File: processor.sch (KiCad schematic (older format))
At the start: 47 parts, among them J4 USB_C_Receptacle_USB2.0, Q5 2N7002, Q6 BC817-40, Q7 BC817-40, U3 ESP32-WROOM-32D, U6 USBLC6-2SC6, U7 TPS560200, U8 CP2102N-A01-GQFN24

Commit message: Clean up rescued symbols and reneabled layer visibility
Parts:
- J4: symbol stack-light-rescue:USB_C_Receptacle_USB2.0-Connector -> Connector:USB_C_Receptacle_USB2.0
- U6: symbol stack-light-rescue:USBLC6-2SC6-Power_Protection -> Power_Protection:USBLC6-2SC6
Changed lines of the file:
@@
 	8800 2000 8800 2100
 $Comp
-L stack-light-rescue:USB_C_Receptacle_USB2.0-Connector J4
+L Connector:USB_C_Receptacle_USB2.0 J4
 U 1 1 5DB0CA37
 P 1650 6500
@@
 Wire Wire Line
 	2250 6400 2250 6500
-Connection ~ 2250 6500
 Wire Wire Line
 	2250 6700 2250 6600
-Connection ~ 2250 6600
 $Comp
 L power:GND #PWR0157
@@
 	2600 6100 2750 6100
 $Comp
-L stack-light-rescue:USBLC6-2SC6-Power_Protection U6
+L Power_Protection:USBLC6-2SC6 U6
 U 1 1 6039A5CC
 P 3150 7050
@@
 	2250 6600 3650 6600
 Wire Wire Line
-	3150 5900 3150 6550
-Wire Wire Line
 	3650 6950 3650 6600
 Wire Wire Line
-	2650 6950 2500 6950
-Wire Wire Line
 	2500 6950 2500 6500
 Wire Wire Line
-	2650 7150 2600 7150
-Wire Wire Line
 	2600 6500 4400 6500
 Wire Wire Line
 	2600 6500 2600 7150
-Wire Wire Line
-	3650 7150 3750 7150
 Wire Wire Line
 	3750 7150 3750 6600
@@
 	1    0    0    -1
 $EndComp
+Wire Wire Line
+	2500 6950 2750 6950
+Wire Wire Line
+	2600 7150 2750 7150
+Wire Wire Line
+	3150 7550 3150 7450
+Wire Wire Line
+	3550 7150 3750 7150
+Wire Wire Line
+	3650 6950 3550 6950
+Wire Wire Line
+	3150 5900 3150 6650
 $EndSCHEMATC

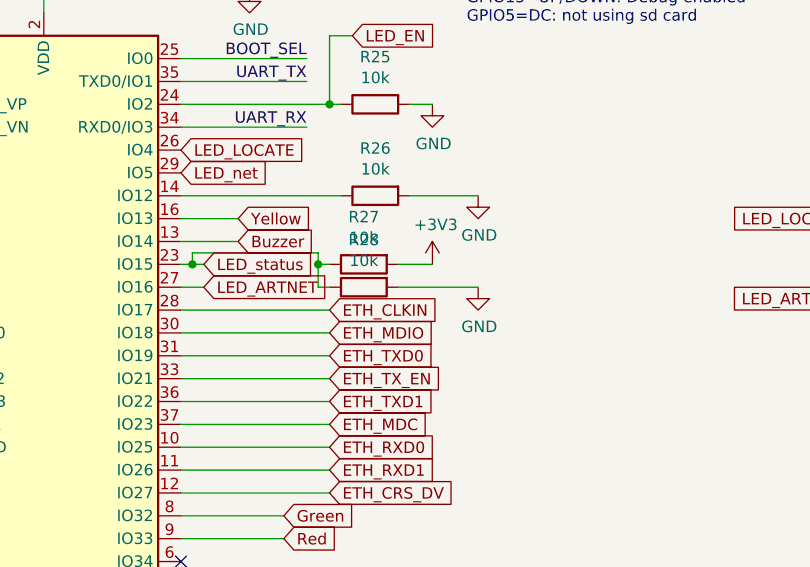
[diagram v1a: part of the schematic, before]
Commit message: Add minor fixes for r1.0 issues
Add load resistors for POE power supply
Add pulldown for buzzer output channel
Mark debug boot resistor as DNP
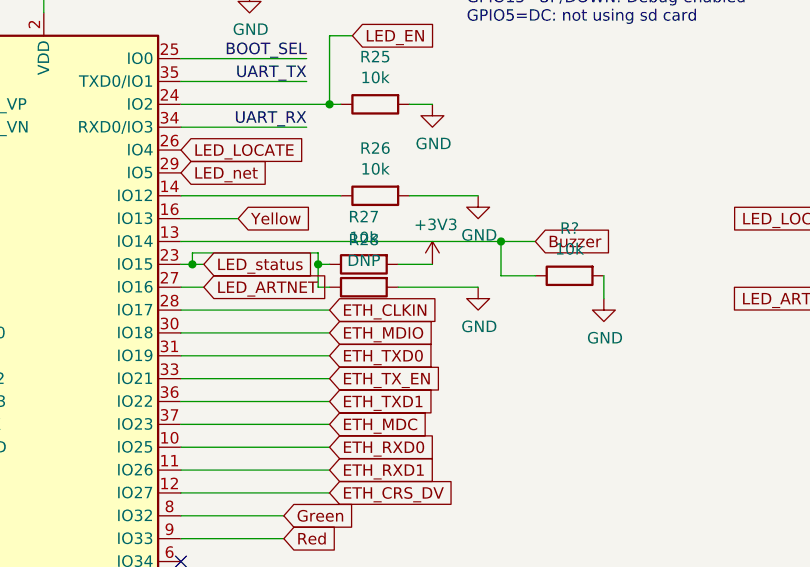
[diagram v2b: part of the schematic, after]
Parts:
- added R?: 10k, Resistor_SMD:R_0603_1608Metric, symbol Device:R
- R28: value 10k -> DNP
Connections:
- net Buzzer: now also R?.1
- net GND: now also R?.2
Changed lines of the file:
@@
 AR Path="/5DEE5ACA/602A9C12" Ref="R28"  Part="1"
 F 0 "R28" V 3693 2400 50  0000 C CNN
-F 1 "10k" V 3784 2400 50  0000 C CNN
+F 1 "DNP" V 3784 2400 50  0000 C CNN
 F 2 "Resistor_SMD:R_0603_1608Metric" V 3830 2400 50  0001 C CNN
 F 3 "~" H 3900 2400 50  0001 C CNN
@@
 Text GLabel 3550 3400 2    50   Input ~ 0
 Green
-Text GLabel 3350 2200 2    50   Input ~ 0
+Text GLabel 4650 2200 2    50   Input ~ 0
 Buzzer
 Text Label 3800 6500 0    50   ~ 0
@@
 	3750 6600 4850 6600
 Wire Wire Line
-	3350 2200 3100 2200
-Wire Wire Line
 	3350 2100 3100 2100
 $Comp
@@
 Wire Wire Line
 	3150 5900 3150 6650
+$Comp
+L Device:R R?
+U 1 1 60A94591
+P 4800 2350
+AR Path="/60A94591" Ref="R?"  Part="1"
+AR Path="/5DEE5ACA/60A94591" Ref="R?"  Part="1"
+F 0 "R?" V 4593 2350 50  0000 C CNN
+F 1 "10k" V 4684 2350 50  0000 C CNN
+F 2 "Resistor_SMD:R_0603_1608Metric" V 4730 2350 50  0001 C CNN
+F 3 "~" H 4800 2350 50  0001 C CNN
+	1    4800 2350
+	0    -1   1    0
+$EndComp
+$Comp
+L power:GND #PWR?
+U 1 1 60A94AE4
+P 4950 2450
+F 0 "#PWR?" H 4950 2200 50  0001 C CNN
+F 1 "GND" H 4955 2277 50  0000 C CNN
+F 2 "" H 4950 2450 50  0001 C CNN
+F 3 "" H 4950 2450 50  0001 C CNN
+	1    4950 2450
+	1    0    0    -1
+$EndComp
+Wire Wire Line
+	4950 2450 4950 2350
+Wire Wire Line
+	4650 2350 4500 2350
+Wire Wire Line
+	4500 2350 4500 2200
+Wire Wire Line
+	4500 2200 4650 2200
+Wire Wire Line
+	3100 2200 4500 2200
+Connection ~ 4500 2200
 $EndSCHEMATC

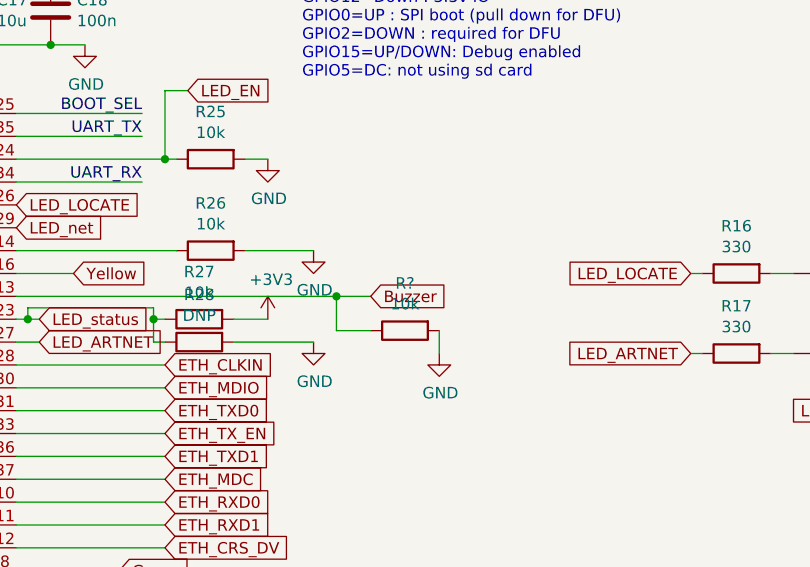
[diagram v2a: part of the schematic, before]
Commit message: Add schematic edits to PCB
Add load resistors for POE power supply
Add pulldown for buzzer output channel
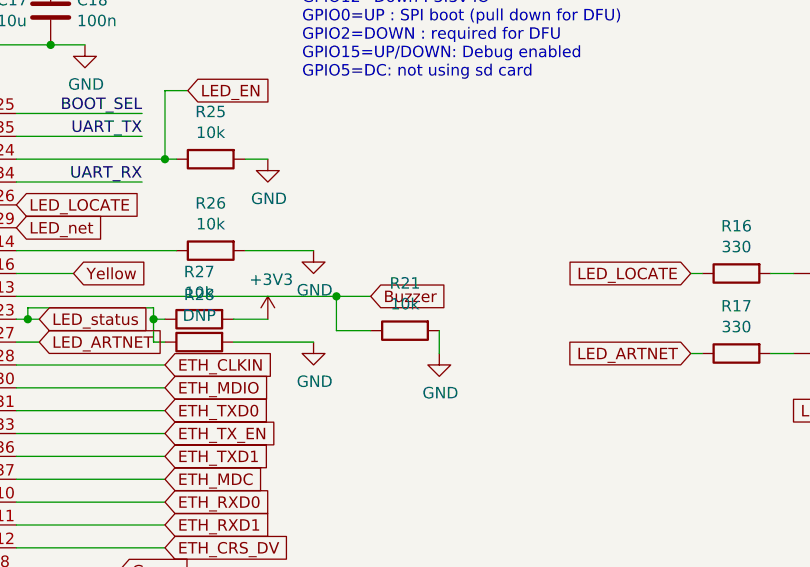
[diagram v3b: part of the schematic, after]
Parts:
- gave numbers to parts that had none: 1
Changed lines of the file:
@@
 P 4800 2350
 AR Path="/60A94591" Ref="R?"  Part="1"
-AR Path="/5DEE5ACA/60A94591" Ref="R?"  Part="1"
-F 0 "R?" V 4593 2350 50  0000 C CNN
+AR Path="/5DEE5ACA/60A94591" Ref="R21"  Part="1"
+F 0 "R21" V 4593 2350 50  0000 C CNN
 F 1 "10k" V 4684 2350 50  0000 C CNN
 F 2 "Resistor_SMD:R_0603_1608Metric" V 4730 2350 50  0001 C CNN
@@
 $EndComp
 $Comp
-L power:GND #PWR?
+L power:GND #PWR0158
 U 1 1 60A94AE4
 P 4950 2450
-F 0 "#PWR?" H 4950 2200 50  0001 C CNN
+F 0 "#PWR0158" H 4950 2200 50  0001 C CNN
 F 1 "GND" H 4955 2277 50  0000 C CNN
 F 2 "" H 4950 2450 50  0001 C CNN

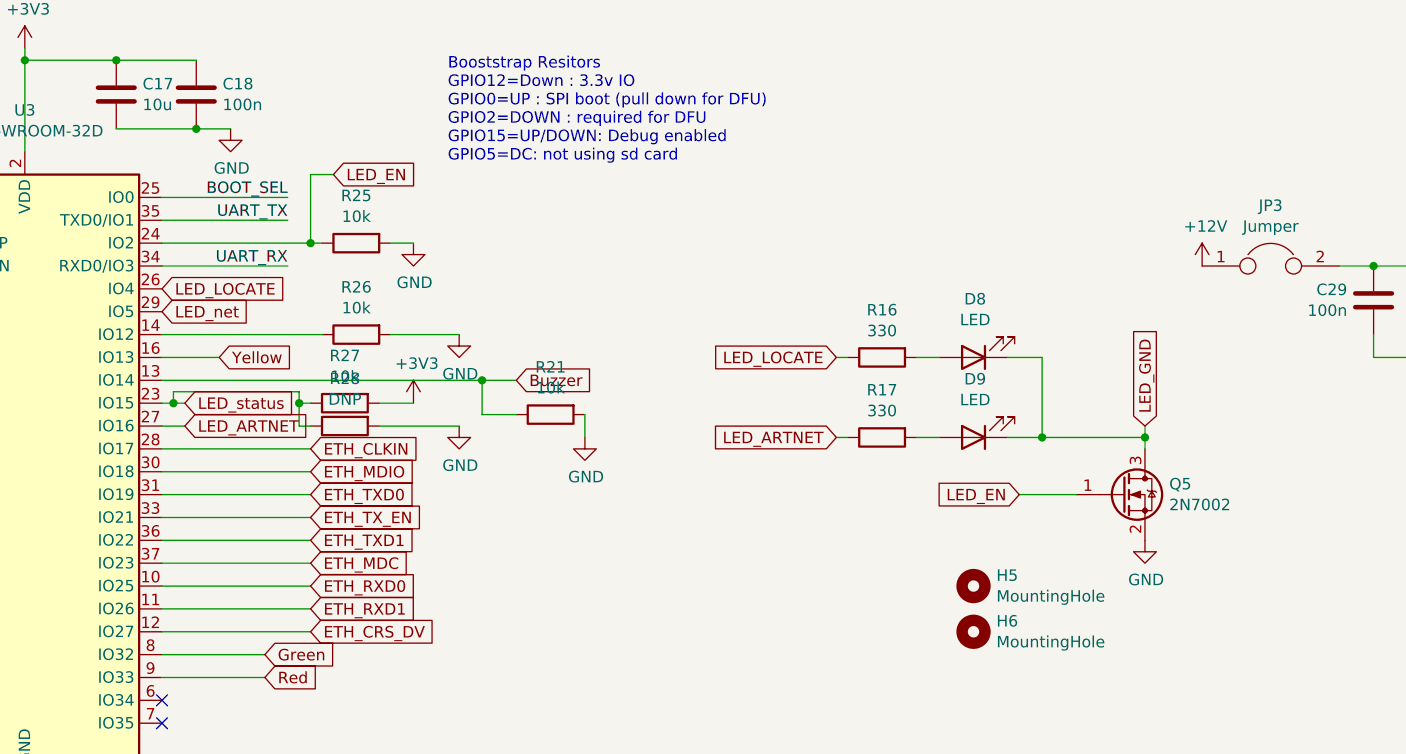
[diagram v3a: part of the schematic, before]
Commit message: Adjust front IO to work with a flush panel
also removed the LED enable transistor
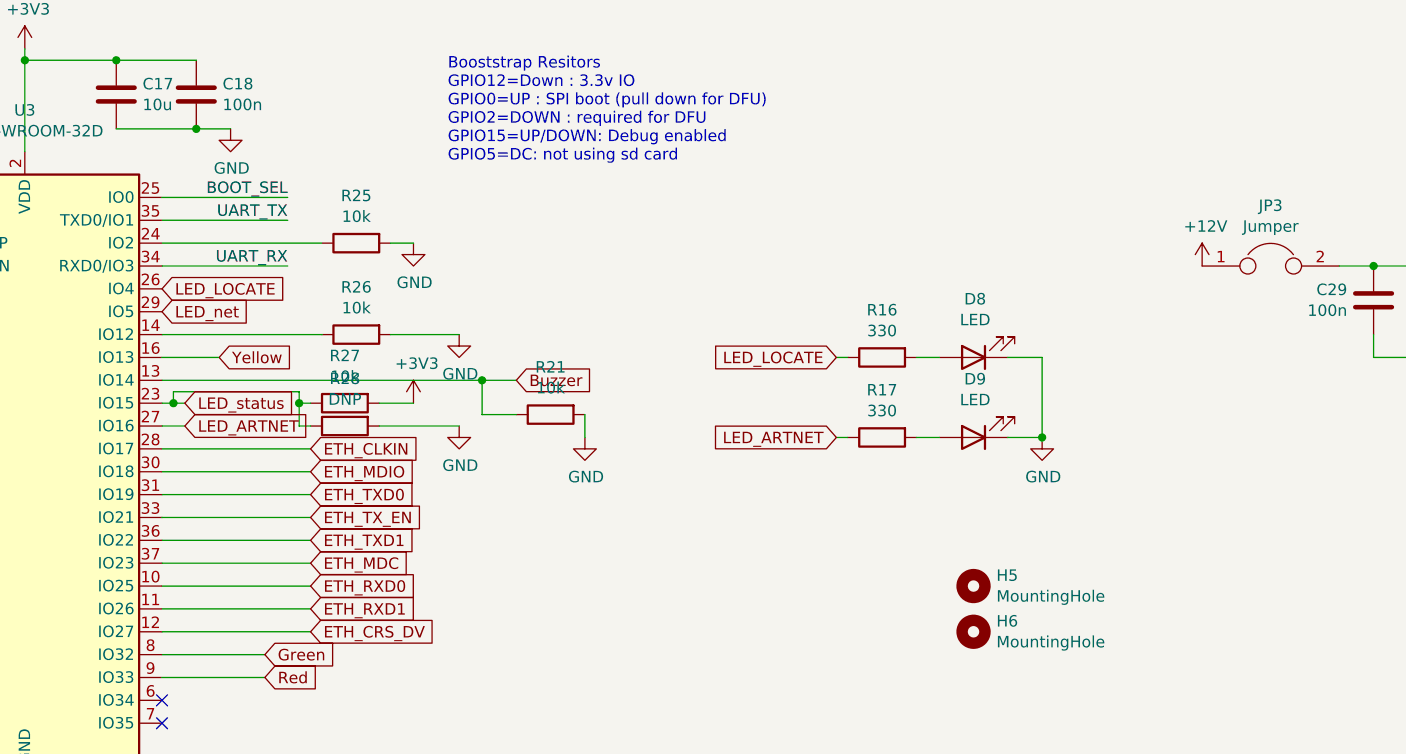
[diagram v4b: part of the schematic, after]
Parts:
- removed Q5: 2N7002, Package_TO_SOT_SMD:SOT-23, symbol Device:Q_NMOS_GSD
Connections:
- net LED_GND is gone; now on net GND: D8.1 (K), D9.1 (K)
- net LED_EN: no longer names the net of R25.1, U3.24 (IO2)
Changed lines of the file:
@@
 	2250 5900 2950 5900
-$Comp
-L Device:Q_NMOS_GSD Q5
-U 1 1 5E7178B7
-P 7300 2700
-F 0 "Q5" H 7506 2746 50  0000 L CNN
-F 1 "2N7002" H 7506 2655 50  0000 L CNN
-F 2 "Package_TO_SOT_SMD:SOT-23" H 7500 2800 50  0001 C CNN
-F 3 "~" H 7300 2700 50  0001 C CNN
-	1    7300 2700
-	1    0    0    -1
-$EndComp
 $Comp
 L power:GND #PWR0164
 U 1 1 5E71A165
-P 7400 2900
-F 0 "#PWR0164" H 7400 2650 50  0001 C CNN
-F 1 "GND" H 7405 2727 50  0000 C CNN
-F 2 "" H 7400 2900 50  0001 C CNN
-F 3 "" H 7400 2900 50  0001 C CNN
-	1    7400 2900
-	1    0    0    -1
-$EndComp
-Text GLabel 7400 2400 1    50   Input ~ 0
-LED_GND
-Wire Wire Line
-	7400 2400 7400 2450
-Text GLabel 6850 2700 0    50   Input ~ 0
-LED_EN
-Wire Wire Line
-	6850 2700 7100 2700
+P 6950 2450
+F 0 "#PWR0164" H 6950 2200 50  0001 C CNN
+F 1 "GND" H 6955 2277 50  0000 C CNN
+F 2 "" H 6950 2450 50  0001 C CNN
+F 3 "" H 6950 2450 50  0001 C CNN
+	1    6950 2450
+	1    0    0    -1
+$EndComp
 $Comp
 L Device:LED D8
@@
 Wire Wire Line
 	6950 2100 6950 2450
-Wire Wire Line
-	6950 2450 7400 2450
-Connection ~ 7400 2450
-Wire Wire Line
-	7400 2450 7400 2500
 Wire Wire Line
 	6800 2450 6950 2450
@@
 Text GLabel 3750 2500 2    50   Input ~ 0
 ETH_CLKIN
-Wire Wire Line
-	3100 1600 3750 1600
 $Comp
 L Device:R R?
@@
 Text GLabel 3100 1800 2    50   Input ~ 0
 LED_LOCATE
-Text GLabel 3850 1300 2    50   Input ~ 0
-LED_EN
-Wire Wire Line
-	3750 1300 3750 1600
-Wire Wire Line
-	3750 1300 3850 1300
-Connection ~ 3750 1600
-Wire Wire Line
-	3750 1600 3800 1600
 NoConn ~ 3100 3600
 NoConn ~ 3100 3700
@@
 	3100 2200 4500 2200
 Connection ~ 4500 2200
+Wire Wire Line
+	3100 1600 3800 1600
 $EndSCHEMATC

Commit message: Add option for SIL regulator module due to component shortage
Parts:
- added U13: TSR_1-2433, Converter_DCDC:Converter_DCDC_TRACO_TSR-1_THT, symbol Regulator_Switching:TSR_1-2433
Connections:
- net +3V3: now also U13.3 (Vout)
- net GND: now also U13.2 (GND)
- net at C29.1, C30.1, JP3.2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: now also U13.1 (Vin)
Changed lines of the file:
@@
 $EndComp
 Wire Wire Line
-	10950 1750 10800 1750
+	10950 1750 10900 1750
 Wire Wire Line
 	10450 1750 10800 1750
@@
 $EndComp
 Wire Wire Line
-	8250 1700 8400 1700
+	8250 1700 8300 1700
 Wire Wire Line
 	8400 1700 8800 1700
@@
 Wire Wire Line
 	3100 1600 3800 1600
+$Comp
+L Regulator_Switching:TSR_1-2433 U13
+U 1 1 6130112F
+P 9300 2900
+F 0 "U13" H 9300 3267 50  0000 C CNN
+F 1 "TSR_1-2433" H 9300 3176 50  0000 C CNN
+F 2 "Converter_DCDC:Converter_DCDC_TRACO_TSR-1_THT" H 9300 2750 50  0001 L CIN
+F 3 "http://www.tracopower.com/products/tsr1.pdf" H 9300 2900 50  0001 C CNN
+	1    9300 2900
+	1    0    0    -1
+$EndComp
+Wire Wire Line
+	8300 1700 8300 2800
+Wire Wire Line
+	8300 2800 8900 2800
+Connection ~ 8300 1700
+Wire Wire Line
+	8300 1700 8400 1700
+Wire Wire Line
+	9700 2800 10900 2800
+Wire Wire Line
+	10900 2800 10900 1750
+Connection ~ 10900 1750
+Wire Wire Line
+	10900 1750 10800 1750
+$Comp
+L power:GND #PWR?
+U 1 1 6130FCEF
+P 9300 3100
+AR Path="/6130FCEF" Ref="#PWR?"  Part="1"
+AR Path="/5DEE5ACA/6130FCEF" Ref="#PWR0161"  Part="1"
+F 0 "#PWR0161" H 9300 2850 50  0001 C CNN
+F 1 "GND" H 9305 2927 50  0000 C CNN
+F 2 "" H 9300 3100 50  0001 C CNN
+F 3 "" H 9300 3100 50  0001 C CNN
+	1    9300 3100
+	1    0    0    -1
+$EndComp
 $EndSCHEMATC
